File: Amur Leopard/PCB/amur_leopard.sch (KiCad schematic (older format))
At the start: 32 parts, among them SW1 SW_Push, U1 ATmega32U4-AU, Y1 16MHz

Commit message: Improve Amur Leopard-PCB & -Schema
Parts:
- MX1, MX2, MX3, MX4, MX5, MX6, MX7, MX8: footprint MX_Only:MXOnly-1U-NoLED -> MX_Alps_Hybrid:MX-1U
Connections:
- net VCC: now also USB1.5 (VBUS); no longer USB1.6 (SHIELD)
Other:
- moved on the sheet: F1
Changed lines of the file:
@@
 L power:VCC #PWR0111
 U 1 1 5F244200
-P 5900 1300
-F 0 "#PWR0111" H 5900 1150 50  0001 C CNN
-F 1 "VCC" H 5917 1473 50  0000 C CNN
-F 2 "" H 5900 1300 50  0001 C CNN
-F 3 "" H 5900 1300 50  0001 C CNN
-	1    5900 1300
+P 5900 1400
+F 0 "#PWR0111" H 5900 1250 50  0001 C CNN
+F 1 "VCC" H 5917 1573 50  0000 C CNN
+F 2 "" H 5900 1400 50  0001 C CNN
+F 3 "" H 5900 1400 50  0001 C CNN
+	1    5900 1400
 	1    0    0    -1
 $EndComp
@@
 L Device:Polyfuse_Small F1
 U 1 1 5F244856
-P 6200 1300
-F 0 "F1" V 5995 1300 50  0000 C CNN
-F 1 "500mA" V 6086 1300 50  0000 C CNN
-F 2 "Fuse:Fuse_1206_3216Metric" H 6250 1100 50  0001 L CNN
-F 3 "~" H 6200 1300 50  0001 C CNN
-	1    6200 1300
+P 6200 1400
+F 0 "F1" V 5995 1400 50  0000 C CNN
+F 1 "500mA" V 6086 1400 50  0000 C CNN
+F 2 "Fuse:Fuse_1206_3216Metric" H 6250 1200 50  0001 L CNN
+F 3 "~" H 6200 1400 50  0001 C CNN
+	1    6200 1400
 	0    1    1    0
 $EndComp
@@
 L power:+5V #PWR0112
 U 1 1 5F244E31
-P 6500 1300
-F 0 "#PWR0112" H 6500 1150 50  0001 C CNN
-F 1 "+5V" H 6515 1473 50  0000 C CNN
-F 2 "" H 6500 1300 50  0001 C CNN
-F 3 "" H 6500 1300 50  0001 C CNN
-	1    6500 1300
-	1    0    0    -1
-$EndComp
-Wire Wire Line
-	6500 1300 6300 1300
-Wire Wire Line
-	6100 1300 5900 1300
-Connection ~ 5900 1300
-Wire Wire Line
-	5900 1300 5700 1300
+P 6500 1400
+F 0 "#PWR0112" H 6500 1250 50  0001 C CNN
+F 1 "+5V" H 6515 1573 50  0000 C CNN
+F 2 "" H 6500 1400 50  0001 C CNN
+F 3 "" H 6500 1400 50  0001 C CNN
+	1    6500 1400
+	1    0    0    -1
+$EndComp
+Wire Wire Line
+	6500 1400 6300 1400
+Wire Wire Line
+	6100 1400 5900 1400
+Connection ~ 5900 1400
+Wire Wire Line
+	5900 1400 5700 1400
 Text GLabel 5700 1500 2    50   Input ~ 0
 D-
@@
 F 0 "MX1" H 7983 3323 60  0000 C CNN
 F 1 "MX-NoLED" H 7983 3249 20  0000 C CNN
-F 2 "MX_Only:MXOnly-1U-NoLED" H 7325 3075 60  0001 C CNN
+F 2 "MX_Alps_Hybrid:MX-1U" H 7325 3075 60  0001 C CNN
 F 3 "" H 7325 3075 60  0001 C CNN
 	1    7950 3100
@@
 F 0 "MX2" H 8533 3323 60  0000 C CNN
 F 1 "MX-NoLED" H 8533 3249 20  0000 C CNN
-F 2 "MX_Only:MXOnly-1U-NoLED" H 7875 3075 60  0001 C CNN
+F 2 "MX_Alps_Hybrid:MX-1U" H 7875 3075 60  0001 C CNN
 F 3 "" H 7875 3075 60  0001 C CNN
 	1    8500 3100
@@
 F 0 "MX3" H 9083 3323 60  0000 C CNN
 F 1 "MX-NoLED" H 9083 3249 20  0000 C CNN
-F 2 "MX_Only:MXOnly-1U-NoLED" H 8425 3075 60  0001 C CNN
+F 2 "MX_Alps_Hybrid:MX-1U" H 8425 3075 60  0001 C CNN
 F 3 "" H 8425 3075 60  0001 C CNN
 	1    9050 3100
@@
 F 0 "MX4" H 9633 3323 60  0000 C CNN
 F 1 "MX-NoLED" H 9633 3249 20  0000 C CNN
-F 2 "MX_Only:MXOnly-1U-NoLED" H 8975 3075 60  0001 C CNN
+F 2 "MX_Alps_Hybrid:MX-1U" H 8975 3075 60  0001 C CNN
 F 3 "" H 8975 3075 60  0001 C CNN
 	1    9600 3100
@@
 F 0 "MX5" H 7983 4073 60  0000 C CNN
 F 1 "MX-NoLED" H 7983 3999 20  0000 C CNN
-F 2 "MX_Only:MXOnly-1U-NoLED" H 7325 3825 60  0001 C CNN
+F 2 "MX_Alps_Hybrid:MX-1U" H 7325 3825 60  0001 C CNN
 F 3 "" H 7325 3825 60  0001 C CNN
 	1    7950 3850
@@
 F 0 "MX6" H 8533 4073 60  0000 C CNN
 F 1 "MX-NoLED" H 8533 3999 20  0000 C CNN
-F 2 "MX_Only:MXOnly-1U-NoLED" H 7875 3825 60  0001 C CNN
+F 2 "MX_Alps_Hybrid:MX-1U" H 7875 3825 60  0001 C CNN
 F 3 "" H 7875 3825 60  0001 C CNN
 	1    8500 3850
@@
 F 0 "MX7" H 9083 4073 60  0000 C CNN
 F 1 "MX-NoLED" H 9083 3999 20  0000 C CNN
-F 2 "MX_Only:MXOnly-1U-NoLED" H 8425 3825 60  0001 C CNN
+F 2 "MX_Alps_Hybrid:MX-1U" H 8425 3825 60  0001 C CNN
 F 3 "" H 8425 3825 60  0001 C CNN
 	1    9050 3850
@@
 F 0 "MX8" H 9633 4073 60  0000 C CNN
 F 1 "MX-NoLED" H 9633 3999 20  0000 C CNN
-F 2 "MX_Only:MXOnly-1U-NoLED" H 8975 3825 60  0001 C CNN
+F 2 "MX_Alps_Hybrid:MX-1U" H 8975 3825 60  0001 C CNN
 F 3 "" H 8975 3825 60  0001 C CNN
 	1    9600 3850

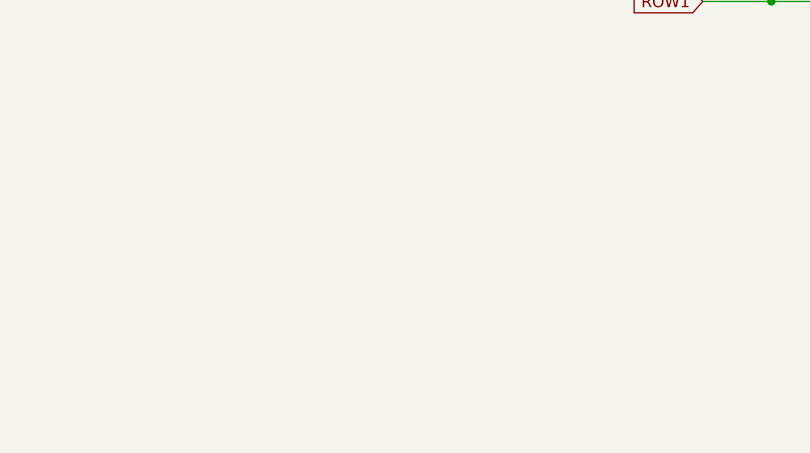
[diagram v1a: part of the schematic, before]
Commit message: Add MountingHoles to Amur Leopard
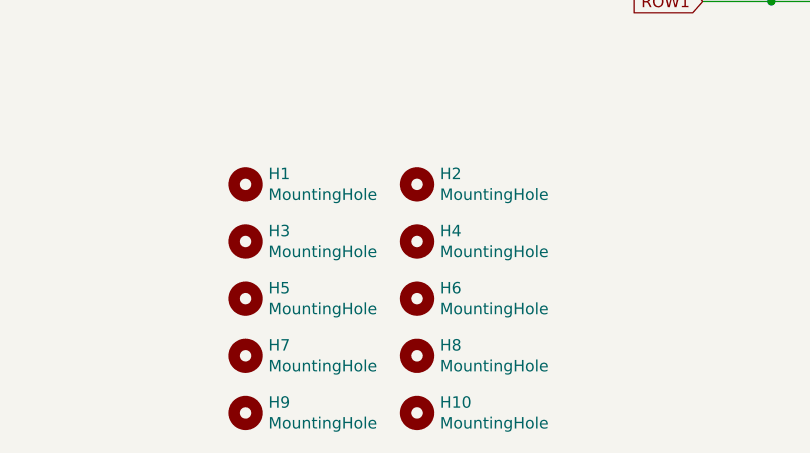
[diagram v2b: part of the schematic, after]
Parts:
- added H1, H10, H2, H3, H4, H5, H6, H7, H8, H9: MountingHole, MountingHole:MountingHole_2mm, symbol Mechanical:MountingHole
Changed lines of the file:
@@
 Text GLabel 4300 3250 2    50   Input ~ 0
 COL3
+$Comp
+L Mechanical:MountingHole H1
+U 1 1 5F2434FA
+P 5500 5000
+F 0 "H1" H 5600 5046 50  0000 L CNN
+F 1 "MountingHole" H 5600 4955 50  0000 L CNN
+F 2 "MountingHole:MountingHole_2mm" H 5500 5000 50  0001 C CNN
+F 3 "~" H 5500 5000 50  0001 C CNN
+	1    5500 5000
+	1    0    0    -1
+$EndComp
+$Comp
+L Mechanical:MountingHole H2
+U 1 1 5F243CC1
+P 6250 5000
+F 0 "H2" H 6350 5046 50  0000 L CNN
+F 1 "MountingHole" H 6350 4955 50  0000 L CNN
+F 2 "MountingHole:MountingHole_2mm" H 6250 5000 50  0001 C CNN
+F 3 "~" H 6250 5000 50  0001 C CNN
+	1    6250 5000
+	1    0    0    -1
+$EndComp
+$Comp
+L Mechanical:MountingHole H3
+U 1 1 5F245A7D
+P 5500 5250
+F 0 "H3" H 5600 5296 50  0000 L CNN
+F 1 "MountingHole" H 5600 5205 50  0000 L CNN
+F 2 "MountingHole:MountingHole_2mm" H 5500 5250 50  0001 C CNN
+F 3 "~" H 5500 5250 50  0001 C CNN
+	1    5500 5250
+	1    0    0    -1
+$EndComp
+$Comp
+L Mechanical:MountingHole H4
+U 1 1 5F245A83
+P 6250 5250
+F 0 "H4" H 6350 5296 50  0000 L CNN
+F 1 "MountingHole" H 6350 5205 50  0000 L CNN
+F 2 "MountingHole:MountingHole_2mm" H 6250 5250 50  0001 C CNN
+F 3 "~" H 6250 5250 50  0001 C CNN
+	1    6250 5250
+	1    0    0    -1
+$EndComp
+$Comp
+L Mechanical:MountingHole H5
+U 1 1 5F247091
+P 5500 5500
+F 0 "H5" H 5600 5546 50  0000 L CNN
+F 1 "MountingHole" H 5600 5455 50  0000 L CNN
+F 2 "MountingHole:MountingHole_2mm" H 5500 5500 50  0001 C CNN
+F 3 "~" H 5500 5500 50  0001 C CNN
+	1    5500 5500
+	1    0    0    -1
+$EndComp
+$Comp
+L Mechanical:MountingHole H6
+U 1 1 5F247097
+P 6250 5500
+F 0 "H6" H 6350 5546 50  0000 L CNN
+F 1 "MountingHole" H 6350 5455 50  0000 L CNN
+F 2 "MountingHole:MountingHole_2mm" H 6250 5500 50  0001 C CNN
+F 3 "~" H 6250 5500 50  0001 C CNN
+	1    6250 5500
+	1    0    0    -1
+$EndComp
+$Comp
+L Mechanical:MountingHole H7
+U 1 1 5F24884F
+P 5500 5750
+F 0 "H7" H 5600 5796 50  0000 L CNN
+F 1 "MountingHole" H 5600 5705 50  0000 L CNN
+F 2 "MountingHole:MountingHole_2mm" H 5500 5750 50  0001 C CNN
+F 3 "~" H 5500 5750 50  0001 C CNN
+	1    5500 5750
+	1    0    0    -1
+$EndComp
+$Comp
+L Mechanical:MountingHole H8
+U 1 1 5F248855
+P 6250 5750
+F 0 "H8" H 6350 5796 50  0000 L CNN
+F 1 "MountingHole" H 6350 5705 50  0000 L CNN
+F 2 "MountingHole:MountingHole_2mm" H 6250 5750 50  0001 C CNN
+F 3 "~" H 6250 5750 50  0001 C CNN
+	1    6250 5750
+	1    0    0    -1
+$EndComp
+$Comp
+L Mechanical:MountingHole H9
+U 1 1 5F24B71B
+P 5500 6000
+F 0 "H9" H 5600 6046 50  0000 L CNN
+F 1 "MountingHole" H 5600 5955 50  0000 L CNN
+F 2 "MountingHole:MountingHole_2mm" H 5500 6000 50  0001 C CNN
+F 3 "~" H 5500 6000 50  0001 C CNN
+	1    5500 6000
+	1    0    0    -1
+$EndComp
+$Comp
+L Mechanical:MountingHole H10
+U 1 1 5F24B721
+P 6250 6000
+F 0 "H10" H 6350 6046 50  0000 L CNN
+F 1 "MountingHole" H 6350 5955 50  0000 L CNN
+F 2 "MountingHole:MountingHole_2mm" H 6250 6000 50  0001 C CNN
+F 3 "~" H 6250 6000 50  0001 C CNN
+	1    6250 6000
+	1    0    0    -1
+$EndComp
 $EndSCHEMATC
